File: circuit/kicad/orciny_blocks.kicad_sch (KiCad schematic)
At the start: 0 parts

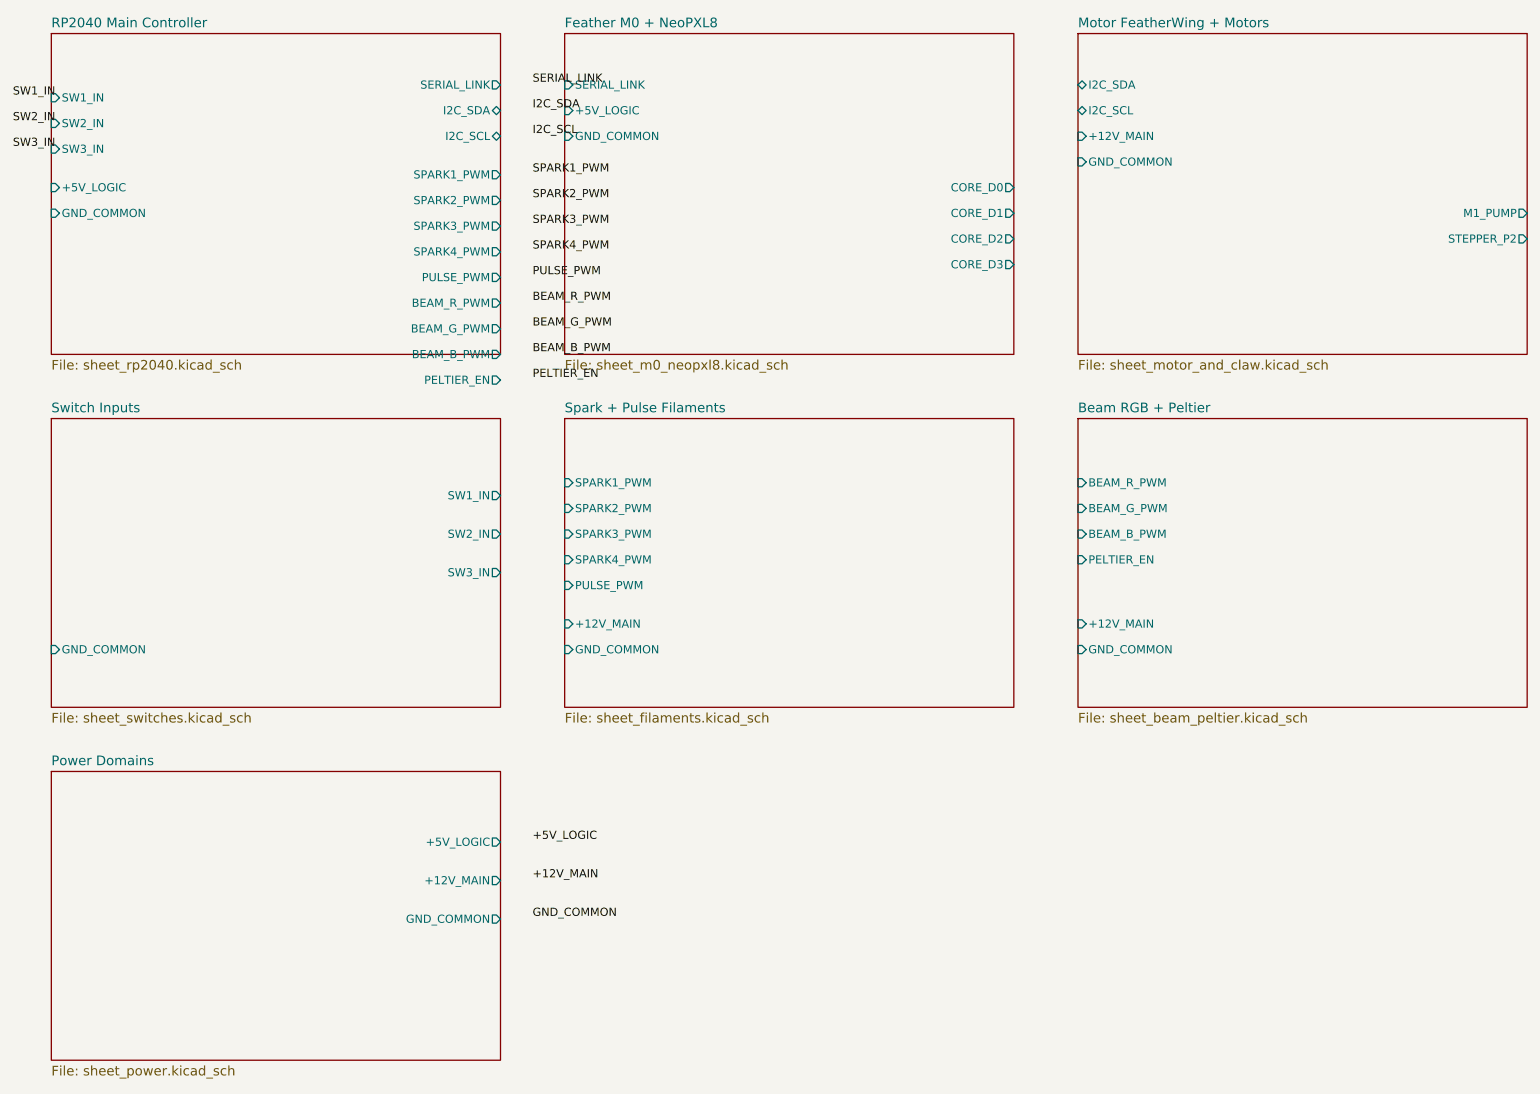
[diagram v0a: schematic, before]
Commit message: Migrate Orciny device to single-strip core and GPIO pump control
Replace the M0 NeoPXL8-based core controller with a single 30-pixel NeoPixel strip on D13 and keep Serial1 TX dedicated to RP2040 effect commands.

Replace Motor FeatherWing pump control with direct RP2040 GP8 MOSFET drive while keeping GP7 assigned to the FP-S14B claw servo.

Update both firmware sketches and DeviceConfig headers to match the revised controller responsibilities, serial command flow, and output mappings.

Restructure the KiCad project by removing the legacy NeoPXL8 and motor-and-claw sheets, adding the new core-strip and pump-and-claw sheets, and aligning the block hierarchy and power sheet with the current 5V bus plus 3V filament rail model.

Synchronize README, ASCII wiring, Mermaid wiring, Fritzing mapping, wire labels, KiCad netmaps, and BOM so the documented hardware revision matches the firmware and schematics.

Standardize beam and filament resistor values across the documentation and KiCad sources and retain a compatibility copy of the older KiCad netmap without leaving contradictory power-rail guidance.
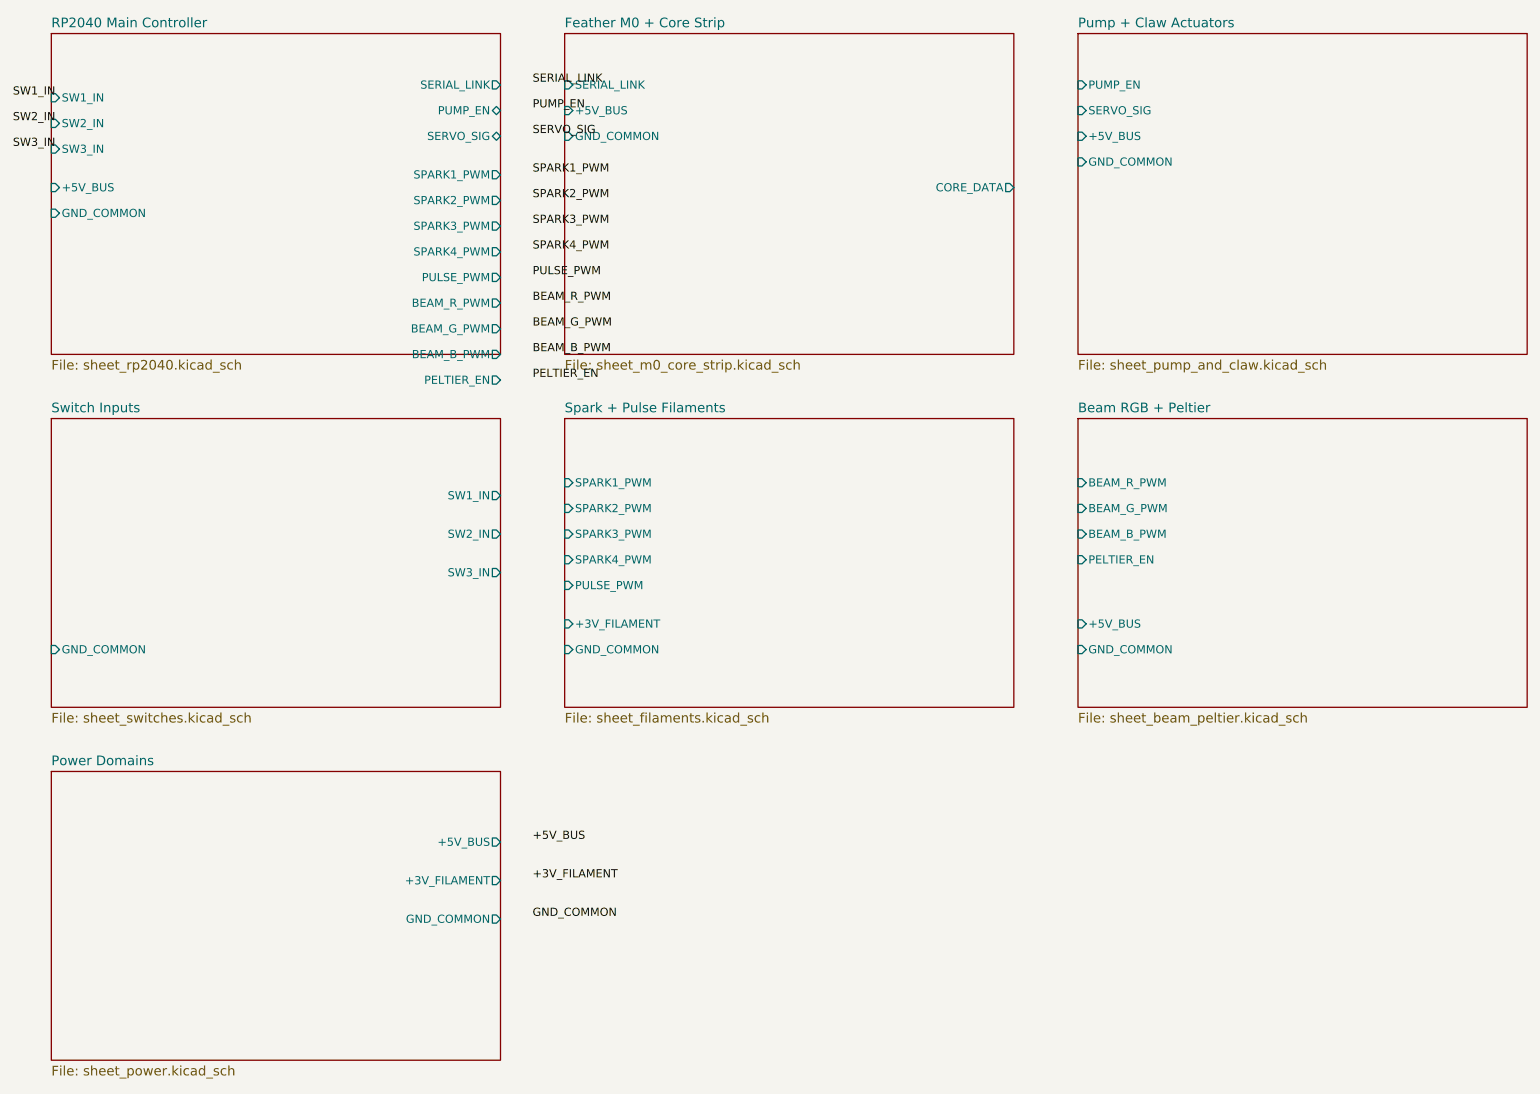
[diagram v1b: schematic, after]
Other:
- sheet Feather M0 + NeoPXL8 renamed Feather M0 + Core Strip
- sheet Motor FeatherWing + Motors renamed Pump + Claw Actuators
- sheet Beam RGB + Peltier ports: added +5V_BUS; removed +12V_MAIN
- sheet Feather M0 + Core Strip: file sheet_m0_neopxl8.kicad_sch -> sheet_m0_core_strip.kicad_sch
- sheet Feather M0 + Core Strip ports: added +5V_BUS, CORE_DATA; removed +5V_LOGIC, CORE_D0, CORE_D1, CORE_D2, CORE_D3
- sheet Power Domains ports: added +3V_FILAMENT, +5V_BUS; removed +12V_MAIN, +5V_LOGIC
- sheet Pump + Claw Actuators: file sheet_motor_and_claw.kicad_sch -> sheet_pump_and_claw.kicad_sch
- sheet Pump + Claw Actuators ports: added +5V_BUS, PUMP_EN, SERVO_SIG; removed +12V_MAIN, I2C_SCL, I2C_SDA, M1_PUMP, STEPPER_P2
- sheet RP2040 Main Controller ports: added +5V_BUS, PUMP_EN, SERVO_SIG; removed +5V_LOGIC, I2C_SCL, I2C_SDA
- sheet Spark + Pulse Filaments ports: added +3V_FILAMENT; removed +12V_MAIN
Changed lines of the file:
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@@
       (effects (font (size 1.27 1.27)) (justify right))
     )
-    (pin "I2C_SDA" bidirectional (at 90.00 32.00 0)
-      (effects (font (size 1.27 1.27)) (justify right))
-    )
-    (pin "I2C_SCL" bidirectional (at 90.00 36.00 0)
+    (pin "PUMP_EN" bidirectional (at 90.00 32.00 0)
+      (effects (font (size 1.27 1.27)) (justify right))
+    )
+    (pin "SERVO_SIG" bidirectional (at 90.00 36.00 0)
       (effects (font (size 1.27 1.27)) (justify right))
     )
@@
       (effects (font (size 1.27 1.27)) (justify right))
     )
-    (pin "+5V_LOGIC" input (at 20.00 44.00 180)
+    (pin "+5V_BUS" input (at 20.00 44.00 180)
       (effects (font (size 1.27 1.27)) (justify left))
     )
@@
     (stroke (width 0) (type solid) (color 0 0 0 0))
     (fill (color 0 0 0 0.0000))
-    (property "Sheet name" "Feather M0 + NeoPXL8" (id 0) (at 100.00 19.20 0)
-      (effects (font (size 1.50 1.50)) (justify left bottom))
-    )
-    (property "Sheet file" "sheet_m0_neopxl8.kicad_sch" (id 1) (at 100.00 70.80 0)
+    (property "Sheet name" "Feather M0 + Core Strip" (id 0) (at 100.00 19.20 0)
+      (effects (font (size 1.50 1.50)) (justify left bottom))
+    )
+    (property "Sheet file" "sheet_m0_core_strip.kicad_sch" (id 1) (at 100.00 70.80 0)
       (effects (font (size 1.50 1.50)) (justify left top))
     )
@@
       (effects (font (size 1.27 1.27)) (justify left))
     )
-    (pin "+5V_LOGIC" input (at 100.00 32.00 180)
+    (pin "+5V_BUS" input (at 100.00 32.00 180)
       (effects (font (size 1.27 1.27)) (justify left))
     )
@@
       (effects (font (size 1.27 1.27)) (justify left))
     )
-    (pin "CORE_D0" output (at 170.00 44.00 0)
-      (effects (font (size 1.27 1.27)) (justify right))
-    )
-    (pin "CORE_D1" output (at 170.00 48.00 0)
-      (effects (font (size 1.27 1.27)) (justify right))
-    )
-    (pin "CORE_D2" output (at 170.00 52.00 0)
-      (effects (font (size 1.27 1.27)) (justify right))
-    )
-    (pin "CORE_D3" output (at 170.00 56.00 0)
+    (pin "CORE_DATA" output (at 170.00 44.00 0)
       (effects (font (size 1.27 1.27)) (justify right))
     )
@@
     (stroke (width 0) (type solid) (color 0 0 0 0))
     (fill (color 0 0 0 0.0000))
-    (property "Sheet name" "Motor FeatherWing + Motors" (id 0) (at 180.00 19.20 0)
-      (effects (font (size 1.50 1.50)) (justify left bottom))
-    )
-    (property "Sheet file" "sheet_motor_and_claw.kicad_sch" (id 1) (at 180.00 70.80 0)
-      (effects (font (size 1.50 1.50)) (justify left top))
-    )
-    (pin "I2C_SDA" bidirectional (at 180.00 28.00 180)
-      (effects (font (size 1.27 1.27)) (justify left))
-    )
-    (pin "I2C_SCL" bidirectional (at 180.00 32.00 180)
-      (effects (font (size 1.27 1.27)) (justify left))
-    )
-    (pin "+12V_MAIN" input (at 180.00 36.00 180)
+    (property "Sheet name" "Pump + Claw Actuators" (id 0) (at 180.00 19.20 0)
+      (effects (font (size 1.50 1.50)) (justify left bottom))
+    )
+    (property "Sheet file" "sheet_pump_and_claw.kicad_sch" (id 1) (at 180.00 70.80 0)
+      (effects (font (size 1.50 1.50)) (justify left top))
+    )
+    (pin "PUMP_EN" input (at 180.00 28.00 180)
+      (effects (font (size 1.27 1.27)) (justify left))
+    )
+    (pin "SERVO_SIG" input (at 180.00 32.00 180)
+      (effects (font (size 1.27 1.27)) (justify left))
+    )
+    (pin "+5V_BUS" input (at 180.00 36.00 180)
       (effects (font (size 1.27 1.27)) (justify left))
     )
@@
       (effects (font (size 1.27 1.27)) (justify left))
     )
-    (pin "M1_PUMP" output (at 250.00 48.00 0)
-      (effects (font (size 1.27 1.27)) (justify right))
-    )
-    (pin "STEPPER_P2" output (at 250.00 52.00 0)
-      (effects (font (size 1.27 1.27)) (justify right))
-    )
   )
   (sheet (at 20.00 80.00) (size 70.00 45.00)
@@
       (effects (font (size 1.27 1.27)) (justify left))
     )
-    (pin "+12V_MAIN" input (at 100.00 112.00 180)
+    (pin "+3V_FILAMENT" input (at 100.00 112.00 180)
       (effects (font (size 1.27 1.27)) (justify left))
     )
@@
       (effects (font (size 1.27 1.27)) (justify left))
     )
-    (pin "+12V_MAIN" input (at 180.00 112.00 180)
+    (pin "+5V_BUS" input (at 180.00 112.00 180)
       (effects (font (size 1.27 1.27)) (justify left))
     )
@@
       (effects (font (size 1.50 1.50)) (justify left top))
     )
-    (pin "+5V_LOGIC" output (at 90.00 146.00 0)
-      (effects (font (size 1.27 1.27)) (justify right))
-    )
-    (pin "+12V_MAIN" output (at 90.00 152.00 0)
+    (pin "+5V_BUS" output (at 90.00 146.00 0)
+      (effects (font (size 1.27 1.27)) (justify right))
+    )
+    (pin "+3V_FILAMENT" output (at 90.00 152.00 0)
       (effects (font (size 1.27 1.27)) (justify right))
     )
@@
     (effects (font (size 1.27 1.27)) (justify left bottom))
   )
-  (label "I2C_SDA" (at 95.00 32.00 0)
-    (effects (font (size 1.27 1.27)) (justify left bottom))
-  )
-  (label "I2C_SCL" (at 95.00 36.00 0)
+  (label "PUMP_EN" (at 95.00 32.00 0)
+    (effects (font (size 1.27 1.27)) (justify left bottom))
+  )
+  (label "SERVO_SIG" (at 95.00 36.00 0)
     (effects (font (size 1.27 1.27)) (justify left bottom))
   )
@@
     (effects (font (size 1.27 1.27)) (justify left bottom))
   )
-  (label "+5V_LOGIC" (at 95.00 146.00 0)
-    (effects (font (size 1.27 1.27)) (justify left bottom))
-  )
-  (label "+12V_MAIN" (at 95.00 152.00 0)
-    (effects (font (size 1.27 1.27)) (justify left bottom))
-  )
+  (label "+5V_BUS" (at 95.00 146.00 0)
+    (effects (font (size 1.27 1.27)) (justify left bottom))
+  )
+  (label "+3V_FILAMENT" (at 95.00 152.00 0)
+    (effects (font (size 1.27 1.27)) (justify left bottom))
+  )
